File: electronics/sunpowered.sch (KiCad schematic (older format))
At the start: 3 parts

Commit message: sunpowered - variable voltage input
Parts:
- removed RL?: FINDER-36.11-4301, symbol FINDER-36.11-4301
- added C?: CP2, symbol CP2
- added D?: ZENER, symbol ZENER
- added RL?: FINDER-30.22, symbol FINDER-30.22
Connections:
- net labels added: GNDPWR
- net labels removed: +BATT
- wire segments 3 -> 5
- no-connect marks 0 -> 2
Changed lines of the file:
@@
 L GND #PWR?
 U 1 1 54D4FE11
-P 900 3950
-F 0 "#PWR?" H 900 3700 60  0001 C CNN
-F 1 "GND" H 900 3800 60  0000 C CNN
-F 2 "" H 900 3950 60  0000 C CNN
-F 3 "" H 900 3950 60  0000 C CNN
-	1    900  3950
+P 3900 2050
+F 0 "#PWR?" H 3900 1800 60  0001 C CNN
+F 1 "GND" H 3900 1900 60  0000 C CNN
+F 2 "" H 3900 2050 60  0000 C CNN
+F 3 "" H 3900 2050 60  0000 C CNN
+	1    3900 2050
 	1    0    0    -1
 $EndComp
@@
 Wire Wire Line
 	1750 1750 2000 1750
-Wire Wire Line
-	2500 1750 3050 1750
 $Comp
-L FINDER-36.11-4301 RL?
-U 1 1 54D5046E
+L FINDER-30.22 RL?
+U 1 1 54D52A34
 P 3350 1550
-F 0 "RL?" V 3800 1550 50  0000 L CNN
-F 1 "FINDER-36.11-4301" V 3900 1200 50  0000 L CNN
+F 0 "RL?" V 4100 1200 50  0000 L CNN
+F 1 "FINDER-30.22" V 4250 1000 50  0001 L CNN
 F 2 "" H 3350 1550 60  0000 C CNN
 F 3 "" H 3350 1550 60  0000 C CNN
@@
 	0    1    1    0
 $EndComp
+Wire Wire Line
+	2500 1750 3050 1750
 $Comp
-L +BATT #PWR?
-U 1 1 54D50A58
-P 4650 800
-F 0 "#PWR?" H 4650 650 60  0001 C CNN
-F 1 "+BATT" H 4650 940 60  0000 C CNN
-F 2 "" H 4650 800 60  0000 C CNN
-F 3 "" H 4650 800 60  0000 C CNN
-	1    4650 800
+L GNDPWR #PWR?
+U 1 1 54D52B1A
+P 1350 2150
+F 0 "#PWR?" H 1350 1950 40  0001 C CNN
+F 1 "GNDPWR" H 1350 2020 40  0000 C CNN
+F 2 "" H 1350 2100 60  0000 C CNN
+F 3 "" H 1350 2100 60  0000 C CNN
+	1    1350 2150
 	1    0    0    -1
 $EndComp
+Wire Wire Line
+	1350 2150 3050 2150
+$Comp
+L CP2 C?
+U 1 1 54D52C0E
+P 2500 1950
+F 0 "C?" H 2550 2050 50  0000 L CNN
+F 1 "CP2" H 2550 1850 50  0000 L CNN
+F 2 "" H 2538 1800 30  0000 C CNN
+F 3 "" H 2500 1950 60  0000 C CNN
+	1    2500 1950
+	1    0    0    -1
+$EndComp
+$Comp
+L ZENER D?
+U 1 1 54D52D0F
+P 2850 1950
+F 0 "D?" H 2850 2050 50  0000 C CNN
+F 1 "ZENER" H 2850 1850 50  0001 C CNN
+F 2 "" H 2850 1950 60  0000 C CNN
+F 3 "" H 2850 1950 60  0000 C CNN
+F 4 "OV protection" V 2600 1950 39  0000 C CNN "Note"
+	1    2850 1950
+	0    -1   -1   0
+$EndComp
+Wire Wire Line
+	3900 2050 3650 2050
+NoConn ~ 3650 1850
+NoConn ~ 3650 2250
+Wire Notes Line
+	3400 900  3400 3300
 $EndSCHEMATC

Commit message: scr overvoltage protection added
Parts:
- removed C?: CP2, symbol CP2
- removed D?: DIODE, symbol DIODE
- removed F?: FUSE, symbol FUSE
- added C?: 100n, symbol C
- added C?: 47n, symbol C
- added D? (x2): 12A, symbol DIODESCH
- added F?: 10A, symbol FUSE
- added P? (x2): CONN_01X01, symbol CONN_01X01
- added R?: 1k, symbol R
- added T?: 12A, symbol THYRISTOR
- D?: value ZENER -> 24V
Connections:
- net labels removed: GNDPWR
- wire segments 5 -> 15
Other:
- moved on the sheet: D?, RL?
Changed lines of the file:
@@
 Comment4 ""
 $EndDescr
+Wire Wire Line
+	1750 1750 2000 1750
 $Comp
-L GND #PWR?
-U 1 1 54D4FE11
-P 3900 2050
-F 0 "#PWR?" H 3900 1800 60  0001 C CNN
-F 1 "GND" H 3900 1900 60  0000 C CNN
-F 2 "" H 3900 2050 60  0000 C CNN
-F 3 "" H 3900 2050 60  0000 C CNN
-	1    3900 2050
-	1    0    0    -1
+L FINDER-30.22 RL?
+U 1 1 54D52A34
+P 5250 2050
+F 0 "RL?" V 6000 1700 50  0000 L CNN
+F 1 "FINDER-30.22" V 6150 1500 50  0001 L CNN
+F 2 "" H 5250 2050 60  0000 C CNN
+F 3 "" H 5250 2050 60  0000 C CNN
+	1    5250 2050
+	0    1    1    0
+$EndComp
+Wire Wire Line
+	1350 2650 4950 2650
+$Comp
+L ZENER D?
+U 1 1 54D52D0F
+P 3050 1950
+F 0 "D?" V 3050 2050 50  0000 C CNN
+F 1 "24V" V 2950 2050 50  0000 C CNN
+F 2 "" H 3050 1950 60  0000 C CNN
+F 3 "http://www.mccsemi.com/up_pdf/MMSZ5221-MMSZ5259%28SOD123%29.pdf" H 3050 1950 60  0001 C CNN
+F 4 "OV protection" V 3350 1950 39  0000 C CNN "Note"
+	1    3050 1950
+	0    -1   -1   0
 $EndComp
 $Comp
-L VCC #PWR?
-U 1 1 54D4FF40
-P 1350 1500
-F 0 "#PWR?" H 1350 1350 60  0001 C CNN
-F 1 "VCC" H 1350 1650 60  0000 C CNN
-F 2 "" H 1350 1500 60  0000 C CNN
-F 3 "" H 1350 1500 60  0000 C CNN
-	1    1350 1500
-	1    0    0    -1
+L CONN_01X01 P?
+U 1 1 54D531B0
+P 1150 1750
+F 0 "P?" H 1150 1850 50  0000 C CNN
+F 1 "CONN_01X01" V 1250 1750 50  0001 C CNN
+F 2 "" H 1150 1750 60  0000 C CNN
+F 3 "" H 1150 1750 60  0000 C CNN
+	1    1150 1750
+	-1   0    0    1
+$EndComp
+$Comp
+L CONN_01X01 P?
+U 1 1 54D531ED
+P 1150 2650
+F 0 "P?" H 1150 2750 50  0000 C CNN
+F 1 "CONN_01X01" V 1250 2650 50  0001 C CNN
+F 2 "" H 1150 2650 60  0000 C CNN
+F 3 "" H 1150 2650 60  0000 C CNN
+	1    1150 2650
+	-1   0    0    1
 $EndComp
 $Comp
 L FUSE F?
-U 1 1 54D4FF79
+U 1 1 54D5362E
 P 2250 1750
 F 0 "F?" H 2350 1800 50  0000 C CNN
-F 1 "FUSE" H 2150 1700 50  0000 C CNN
+F 1 "10A" H 2150 1700 50  0000 C CNN
 F 2 "" H 2250 1750 60  0000 C CNN
 F 3 "" H 2250 1750 60  0000 C CNN
@@
 	1    0    0    -1
 $EndComp
+Wire Wire Line
+	4350 1750 4350 2250
+Connection ~ 3050 1750
 $Comp
-L DIODE D?
-U 1 1 54D500EA
+L C C?
+U 1 1 54D539D0
+P 2500 2150
+F 0 "C?" H 2550 2250 50  0000 L CNN
+F 1 "100n" H 2550 2050 50  0000 L CNN
+F 2 "" H 2538 2000 30  0000 C CNN
+F 3 "" H 2500 2150 60  0000 C CNN
+	1    2500 2150
+	1    0    0    -1
+$EndComp
+Wire Wire Line
+	2500 2350 2500 2650
+Connection ~ 2500 2650
+Wire Wire Line
+	2500 1950 2500 1750
+$Comp
+L R R?
+U 1 1 54D53A8D
+P 3050 2400
+F 0 "R?" H 3150 2200 50  0000 C CNN
+F 1 "1k" V 3057 2401 50  0000 C CNN
+F 2 "" V 2980 2400 30  0000 C CNN
+F 3 "" H 3050 2400 30  0000 C CNN
+	1    3050 2400
+	1    0    0    -1
+$EndComp
+Connection ~ 3050 2650
+Connection ~ 2500 1750
+Wire Wire Line
+	4350 2250 4950 2250
+Wire Wire Line
+	3050 2150 3650 2150
+$Comp
+L C C?
+U 1 1 54D53D1F
+P 3400 2350
+F 0 "C?" H 3450 2450 50  0000 L CNN
+F 1 "47n" H 3450 2250 50  0000 L CNN
+F 2 "" H 3438 2200 30  0000 C CNN
+F 3 "" H 3400 2350 60  0000 C CNN
+	1    3400 2350
+	1    0    0    -1
+$EndComp
+Wire Wire Line
+	3400 2550 3400 2650
+Connection ~ 3400 2650
+$Comp
+L THYRISTOR T?
+U 1 1 54D53E05
+P 3800 2050
+F 0 "T?" V 3800 2150 50  0000 C CNN
+F 1 "12A" V 3800 1900 50  0000 C CNN
+F 2 "" H 3800 2050 60  0000 C CNN
+F 3 "http://www.nxp.com/documents/data_sheet/BT151S_SER_L_R.pdf" H 3800 2050 60  0001 C CNN
+	1    3800 2050
+	0    -1   1    0
+$EndComp
+Wire Wire Line
+	3800 1850 3800 1750
+Connection ~ 3800 1750
+Wire Wire Line
+	3800 2250 3800 2650
+Connection ~ 3800 2650
+Connection ~ 3400 2150
+$Comp
+L DIODESCH D?
+U 1 1 54D53F49
 P 1550 1750
 F 0 "D?" H 1550 1850 50  0000 C CNN
-F 1 "DIODE" H 1550 1650 50  0000 C CNN
+F 1 "12A" H 1550 1650 50  0000 C CNN
 F 2 "" H 1550 1750 60  0000 C CNN
-F 3 "" H 1550 1750 60  0000 C CNN
+F 3 "http://www.vishay.com/docs/89094/v12p12.pdf" H 1550 1750 60  0001 C CNN
 	1    1550 1750
 	1    0    0    -1
 $EndComp
-Wire Wire Line
-	1350 1500 1350 1750
-Wire Wire Line
-	1750 1750 2000 1750
 $Comp
-L FINDER-30.22 RL?
-U 1 1 54D52A34
-P 3350 1550
-F 0 "RL?" V 4100 1200 50  0000 L CNN
-F 1 "FINDER-30.22" V 4250 1000 50  0001 L CNN
-F 2 "" H 3350 1550 60  0000 C CNN
-F 3 "" H 3350 1550 60  0000 C CNN
-	1    3350 1550
-	0    1    1    0
-$EndComp
-Wire Wire Line
-	2500 1750 3050 1750
-$Comp
-L GNDPWR #PWR?
-U 1 1 54D52B1A
-P 1350 2150
-F 0 "#PWR?" H 1350 1950 40  0001 C CNN
-F 1 "GNDPWR" H 1350 2020 40  0000 C CNN
-F 2 "" H 1350 2100 60  0000 C CNN
-F 3 "" H 1350 2100 60  0000 C CNN
-	1    1350 2150
+L DIODESCH D?
+U 1 1 54D53FCE
+P 4150 1750
+F 0 "D?" H 4150 1850 50  0000 C CNN
+F 1 "12A" H 4150 1650 50  0000 C CNN
+F 2 "" H 4150 1750 60  0000 C CNN
+F 3 "http://www.vishay.com/docs/89094/v12p12.pdf" H 4150 1750 60  0001 C CNN
+	1    4150 1750
 	1    0    0    -1
 $EndComp
 Wire Wire Line
-	1350 2150 3050 2150
+	2500 1750 3950 1750
 $Comp
-L CP2 C?
-U 1 1 54D52C0E
-P 2500 1950
-F 0 "C?" H 2550 2050 50  0000 L CNN
-F 1 "CP2" H 2550 1850 50  0000 L CNN
-F 2 "" H 2538 1800 30  0000 C CNN
-F 3 "" H 2500 1950 60  0000 C CNN
-	1    2500 1950
+L GND #PWR?
+U 1 1 54D5467F
+P 5850 2550
+F 0 "#PWR?" H 5850 2300 60  0001 C CNN
+F 1 "GND" H 5850 2400 60  0000 C CNN
+F 2 "" H 5850 2550 60  0000 C CNN
+F 3 "" H 5850 2550 60  0000 C CNN
+	1    5850 2550
 	1    0    0    -1
 $EndComp
+Wire Wire Line
+	5850 2550 5550 2550
+Wire Wire Line
+	5550 2350 5600 2350
+Wire Wire Line
+	5550 2750 5600 2750
+NoConn ~ 5600 2350
+NoConn ~ 5600 2750
 $Comp
-L ZENER D?
-U 1 1 54D52D0F
-P 2850 1950
-F 0 "D?" H 2850 2050 50  0000 C CNN
-F 1 "ZENER" H 2850 1850 50  0001 C CNN
-F 2 "" H 2850 1950 60  0000 C CNN
-F 3 "" H 2850 1950 60  0000 C CNN
-F 4 "OV protection" V 2600 1950 39  0000 C CNN "Note"
-	1    2850 1950
-	0    -1   -1   0
+L VCC #PWR?
+U 1 1 54D547B5
+P 5800 2150
+F 0 "#PWR?" H 5800 2000 60  0001 C CNN
+F 1 "VCC" H 5800 2300 60  0000 C CNN
+F 2 "" H 5800 2150 60  0000 C CNN
+F 3 "" H 5800 2150 60  0000 C CNN
+	1    5800 2150
+	1    0    0    -1
 $EndComp
 Wire Wire Line
-	3900 2050 3650 2050
-NoConn ~ 3650 1850
-NoConn ~ 3650 2250
-Wire Notes Line
-	3400 900  3400 3300
+	5800 2150 5550 2150
 $EndSCHEMATC

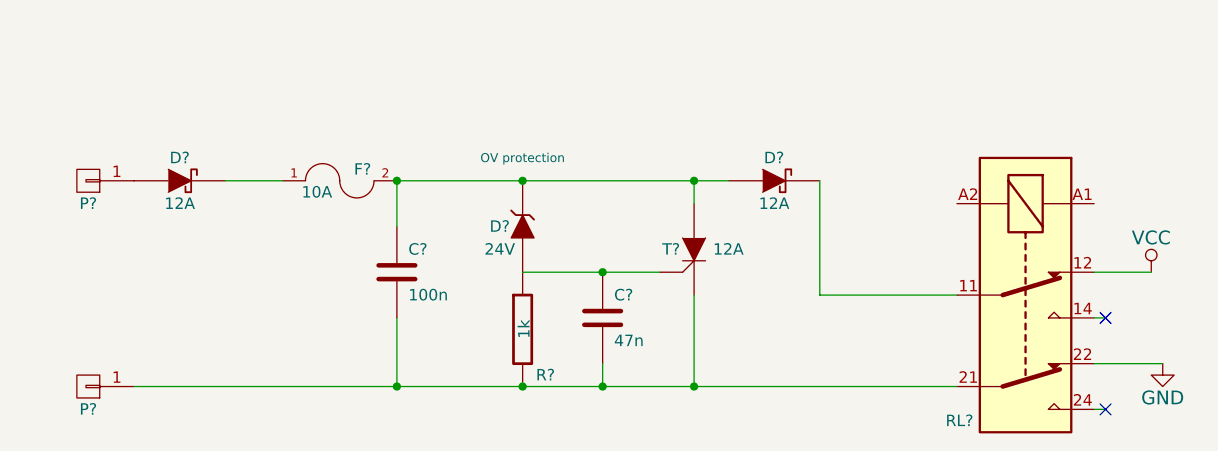
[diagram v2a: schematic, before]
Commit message: manual switch instead of a relay, better over voltage protection
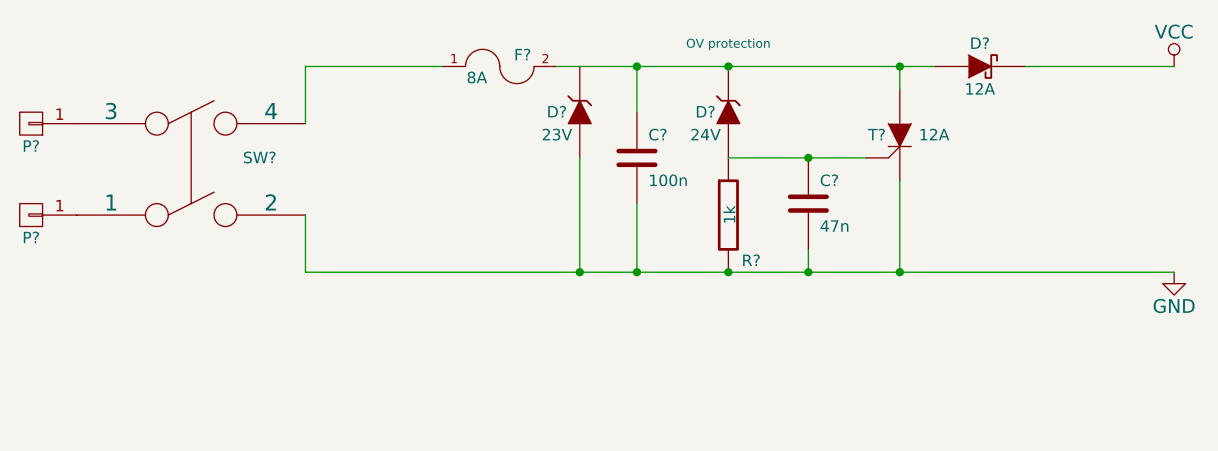
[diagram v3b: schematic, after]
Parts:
- removed D?: 12A, symbol DIODESCH
- removed RL?: FINDER-30.22, symbol FINDER-30.22
- added D?: 23V, symbol ZENER
- added SW?: DPST, symbol DPST
- F?: value 10A -> 8A
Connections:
- net GND: now also C?.2, C?.2, R?.2, T?.K, D?.1 (A), SW?.2
- net VCC: now also D?.2 (K)
- net at P?.1 (P1): now also SW?.3
- net at F?.1: now also SW?.4
- new net: P?.1 (P1), SW?.1
- no-connect marks 2 -> 0
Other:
- moved on the sheet: C?, D?, F?, P?, R?, T?
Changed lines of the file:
@@
 Comment4 ""
 $EndDescr
-Wire Wire Line
-	1750 1750 2000 1750
-$Comp
-L FINDER-30.22 RL?
-U 1 1 54D52A34
-P 5250 2050
-F 0 "RL?" V 6000 1700 50  0000 L CNN
-F 1 "FINDER-30.22" V 6150 1500 50  0001 L CNN
-F 2 "" H 5250 2050 60  0000 C CNN
-F 3 "" H 5250 2050 60  0000 C CNN
-	1    5250 2050
-	0    1    1    0
-$EndComp
-Wire Wire Line
-	1350 2650 4950 2650
 $Comp
 L ZENER D?
 U 1 1 54D52D0F
-P 3050 1950
-F 0 "D?" V 3050 2050 50  0000 C CNN
-F 1 "24V" V 2950 2050 50  0000 C CNN
-F 2 "" H 3050 1950 60  0000 C CNN
-F 3 "http://www.mccsemi.com/up_pdf/MMSZ5221-MMSZ5259%28SOD123%29.pdf" H 3050 1950 60  0001 C CNN
-F 4 "OV protection" V 3350 1950 39  0000 C CNN "Note"
-	1    3050 1950
+P 3950 1450
+F 0 "D?" V 3950 1550 50  0000 C CNN
+F 1 "24V" V 3850 1550 50  0000 C CNN
+F 2 "" H 3950 1450 60  0000 C CNN
+F 3 "http://www.mccsemi.com/up_pdf/MMSZ5221-MMSZ5259%28SOD123%29.pdf" H 3950 1450 60  0001 C CNN
+F 4 "OV protection" V 4250 1450 39  0000 C CNN "Note"
+	1    3950 1450
 	0    -1   -1   0
 $EndComp
@@
 L CONN_01X01 P?
 U 1 1 54D531B0
-P 1150 1750
-F 0 "P?" H 1150 1850 50  0000 C CNN
-F 1 "CONN_01X01" V 1250 1750 50  0001 C CNN
-F 2 "" H 1150 1750 60  0000 C CNN
-F 3 "" H 1150 1750 60  0000 C CNN
-	1    1150 1750
+P 900 1500
+F 0 "P?" H 900 1600 50  0000 C CNN
+F 1 "CONN_01X01" V 1000 1500 50  0001 C CNN
+F 2 "" H 900 1500 60  0000 C CNN
+F 3 "" H 900 1500 60  0000 C CNN
+	1    900  1500
 	-1   0    0    1
 $EndComp
@@
 L CONN_01X01 P?
 U 1 1 54D531ED
-P 1150 2650
-F 0 "P?" H 1150 2750 50  0000 C CNN
-F 1 "CONN_01X01" V 1250 2650 50  0001 C CNN
-F 2 "" H 1150 2650 60  0000 C CNN
-F 3 "" H 1150 2650 60  0000 C CNN
-	1    1150 2650
+P 900 1900
+F 0 "P?" H 900 2000 50  0000 C CNN
+F 1 "CONN_01X01" V 1000 1900 50  0001 C CNN
+F 2 "" H 900 1900 60  0000 C CNN
+F 3 "" H 900 1900 60  0000 C CNN
+	1    900  1900
 	-1   0    0    1
 $EndComp
@@
 L FUSE F?
 U 1 1 54D5362E
-P 2250 1750
-F 0 "F?" H 2350 1800 50  0000 C CNN
-F 1 "10A" H 2150 1700 50  0000 C CNN
-F 2 "" H 2250 1750 60  0000 C CNN
-F 3 "" H 2250 1750 60  0000 C CNN
-	1    2250 1750
+P 2950 1250
+F 0 "F?" H 3050 1300 50  0000 C CNN
+F 1 "8A" H 2850 1200 50  0000 C CNN
+F 2 "" H 2950 1250 60  0000 C CNN
+F 3 "" H 2950 1250 60  0000 C CNN
+	1    2950 1250
+	1    0    0    -1
+$EndComp
+Connection ~ 3950 1250
+$Comp
+L C C?
+U 1 1 54D539D0
+P 3550 1650
+F 0 "C?" H 3600 1750 50  0000 L CNN
+F 1 "100n" H 3600 1550 50  0000 L CNN
+F 2 "" H 3588 1500 30  0000 C CNN
+F 3 "" H 3550 1650 60  0000 C CNN
+	1    3550 1650
+	1    0    0    -1
+$EndComp
+$Comp
+L R R?
+U 1 1 54D53A8D
+P 3950 1900
+F 0 "R?" H 4050 1700 50  0000 C CNN
+F 1 "1k" V 3957 1901 50  0000 C CNN
+F 2 "" V 3880 1900 30  0000 C CNN
+F 3 "" H 3950 1900 30  0000 C CNN
+	1    3950 1900
+	1    0    0    -1
+$EndComp
+Connection ~ 3950 2150
+Wire Wire Line
+	3950 1650 4550 1650
+$Comp
+L C C?
+U 1 1 54D53D1F
+P 4300 1850
+F 0 "C?" H 4350 1950 50  0000 L CNN
+F 1 "47n" H 4350 1750 50  0000 L CNN
+F 2 "" H 4338 1700 30  0000 C CNN
+F 3 "" H 4300 1850 60  0000 C CNN
+	1    4300 1850
 	1    0    0    -1
 $EndComp
 Wire Wire Line
-	4350 1750 4350 2250
-Connection ~ 3050 1750
+	4300 2050 4300 2150
+Connection ~ 4300 2150
 $Comp
-L C C?
-U 1 1 54D539D0
-P 2500 2150
-F 0 "C?" H 2550 2250 50  0000 L CNN
-F 1 "100n" H 2550 2050 50  0000 L CNN
-F 2 "" H 2538 2000 30  0000 C CNN
-F 3 "" H 2500 2150 60  0000 C CNN
-	1    2500 2150
+L THYRISTOR T?
+U 1 1 54D53E05
+P 4700 1550
+F 0 "T?" V 4700 1650 50  0000 C CNN
+F 1 "12A" V 4700 1400 50  0000 C CNN
+F 2 "" H 4700 1550 60  0000 C CNN
+F 3 "http://www.nxp.com/documents/data_sheet/BT151S_SER_L_R.pdf" H 4700 1550 60  0001 C CNN
+	1    4700 1550
+	0    -1   1    0
+$EndComp
+Wire Wire Line
+	4700 1250 4700 1350
+Connection ~ 4700 1250
+Wire Wire Line
+	4700 1750 4700 2150
+Connection ~ 4700 2150
+Connection ~ 4300 1650
+$Comp
+L DIODESCH D?
+U 1 1 54D53FCE
+P 5050 1250
+F 0 "D?" H 5050 1350 50  0000 C CNN
+F 1 "12A" H 5050 1150 50  0000 C CNN
+F 2 "" H 5050 1250 60  0000 C CNN
+F 3 "http://www.vishay.com/docs/89094/v12p12.pdf" H 5050 1250 60  0001 C CNN
+	1    5050 1250
 	1    0    0    -1
 $EndComp
 Wire Wire Line
-	2500 2350 2500 2650
-Connection ~ 2500 2650
-Wire Wire Line
-	2500 1950 2500 1750
+	3200 1250 4850 1250
 $Comp
-L R R?
-U 1 1 54D53A8D
-P 3050 2400
-F 0 "R?" H 3150 2200 50  0000 C CNN
-F 1 "1k" V 3057 2401 50  0000 C CNN
-F 2 "" V 2980 2400 30  0000 C CNN
-F 3 "" H 3050 2400 30  0000 C CNN
-	1    3050 2400
+L GND #PWR?
+U 1 1 54D5467F
+P 5900 2150
+F 0 "#PWR?" H 5900 1900 60  0001 C CNN
+F 1 "GND" H 5900 2000 60  0000 C CNN
+F 2 "" H 5900 2150 60  0000 C CNN
+F 3 "" H 5900 2150 60  0000 C CNN
+	1    5900 2150
 	1    0    0    -1
 $EndComp
-Connection ~ 3050 2650
-Connection ~ 2500 1750
-Wire Wire Line
-	4350 2250 4950 2250
-Wire Wire Line
-	3050 2150 3650 2150
 $Comp
-L C C?
-U 1 1 54D53D1F
-P 3400 2350
-F 0 "C?" H 3450 2450 50  0000 L CNN
-F 1 "47n" H 3450 2250 50  0000 L CNN
-F 2 "" H 3438 2200 30  0000 C CNN
-F 3 "" H 3400 2350 60  0000 C CNN
-	1    3400 2350
+L VCC #PWR?
+U 1 1 54D547B5
+P 5900 1250
+F 0 "#PWR?" H 5900 1100 60  0001 C CNN
+F 1 "VCC" H 5900 1400 60  0000 C CNN
+F 2 "" H 5900 1250 60  0000 C CNN
+F 3 "" H 5900 1250 60  0000 C CNN
+	1    5900 1250
+	1    0    0    -1
+$EndComp
+$Comp
+L DPST SW?
+U 1 1 54D5CEC6
+P 1600 1700
+F 0 "SW?" H 1900 1750 50  0000 C CNN
+F 1 "DPST" H 1900 1650 50  0001 C CNN
+F 2 "" H 1600 1700 60  0000 C CNN
+F 3 "" H 1600 1700 60  0000 C CNN
+	1    1600 1700
 	1    0    0    -1
 $EndComp
 Wire Wire Line
-	3400 2550 3400 2650
-Connection ~ 3400 2650
+	3550 2150 3550 1850
+Connection ~ 3550 2150
+Wire Wire Line
+	3550 1450 3550 1250
+Connection ~ 3550 1250
+Wire Wire Line
+	5250 1250 5900 1250
 $Comp
-L THYRISTOR T?
-U 1 1 54D53E05
-P 3800 2050
-F 0 "T?" V 3800 2150 50  0000 C CNN
-F 1 "12A" V 3800 1900 50  0000 C CNN
-F 2 "" H 3800 2050 60  0000 C CNN
-F 3 "http://www.nxp.com/documents/data_sheet/BT151S_SER_L_R.pdf" H 3800 2050 60  0001 C CNN
-	1    3800 2050
-	0    -1   1    0
+L ZENER D?
+U 1 1 54D5E43B
+P 3300 1450
+F 0 "D?" V 3300 1550 50  0000 C CNN
+F 1 "23V" V 3200 1550 50  0000 C CNN
+F 2 "" H 3300 1450 60  0000 C CNN
+F 3 "" H 3300 1450 60  0000 C CNN
+	1    3300 1450
+	0    -1   -1   0
 $EndComp
 Wire Wire Line
-	3800 1850 3800 1750
-Connection ~ 3800 1750
+	3300 1650 3300 2150
+Connection ~ 3300 2150
 Wire Wire Line
-	3800 2250 3800 2650
-Connection ~ 3800 2650
-Connection ~ 3400 2150
-$Comp
-L DIODESCH D?
-U 1 1 54D53F49
-P 1550 1750
-F 0 "D?" H 1550 1850 50  0000 C CNN
-F 1 "12A" H 1550 1650 50  0000 C CNN
-F 2 "" H 1550 1750 60  0000 C CNN
-F 3 "http://www.vishay.com/docs/89094/v12p12.pdf" H 1550 1750 60  0001 C CNN
-	1    1550 1750
-	1    0    0    -1
-$EndComp
-$Comp
-L DIODESCH D?
-U 1 1 54D53FCE
-P 4150 1750
-F 0 "D?" H 4150 1850 50  0000 C CNN
-F 1 "12A" H 4150 1650 50  0000 C CNN
-F 2 "" H 4150 1750 60  0000 C CNN
-F 3 "http://www.vishay.com/docs/89094/v12p12.pdf" H 4150 1750 60  0001 C CNN
-	1    4150 1750
-	1    0    0    -1
-$EndComp
+	2100 1500 2100 1250
 Wire Wire Line
-	2500 1750 3950 1750
-$Comp
-L GND #PWR?
-U 1 1 54D5467F
-P 5850 2550
-F 0 "#PWR?" H 5850 2300 60  0001 C CNN
-F 1 "GND" H 5850 2400 60  0000 C CNN
-F 2 "" H 5850 2550 60  0000 C CNN
-F 3 "" H 5850 2550 60  0000 C CNN
-	1    5850 2550
-	1    0    0    -1
-$EndComp
+	2100 1250 2700 1250
 Wire Wire Line
-	5850 2550 5550 2550
+	2100 1900 2100 2150
 Wire Wire Line
-	5550 2350 5600 2350
-Wire Wire Line
-	5550 2750 5600 2750
-NoConn ~ 5600 2350
-NoConn ~ 5600 2750
-$Comp
-L VCC #PWR?
-U 1 1 54D547B5
-P 5800 2150
-F 0 "#PWR?" H 5800 2000 60  0001 C CNN
-F 1 "VCC" H 5800 2300 60  0000 C CNN
-F 2 "" H 5800 2150 60  0000 C CNN
-F 3 "" H 5800 2150 60  0000 C CNN
-	1    5800 2150
-	1    0    0    -1
-$EndComp
-Wire Wire Line
-	5800 2150 5550 2150
+	2100 2150 5900 2150
 $EndSCHEMATC
